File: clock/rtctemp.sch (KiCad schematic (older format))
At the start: 15 parts, among them U601 ADT7410, U602 DS3231, U603 ADT7410

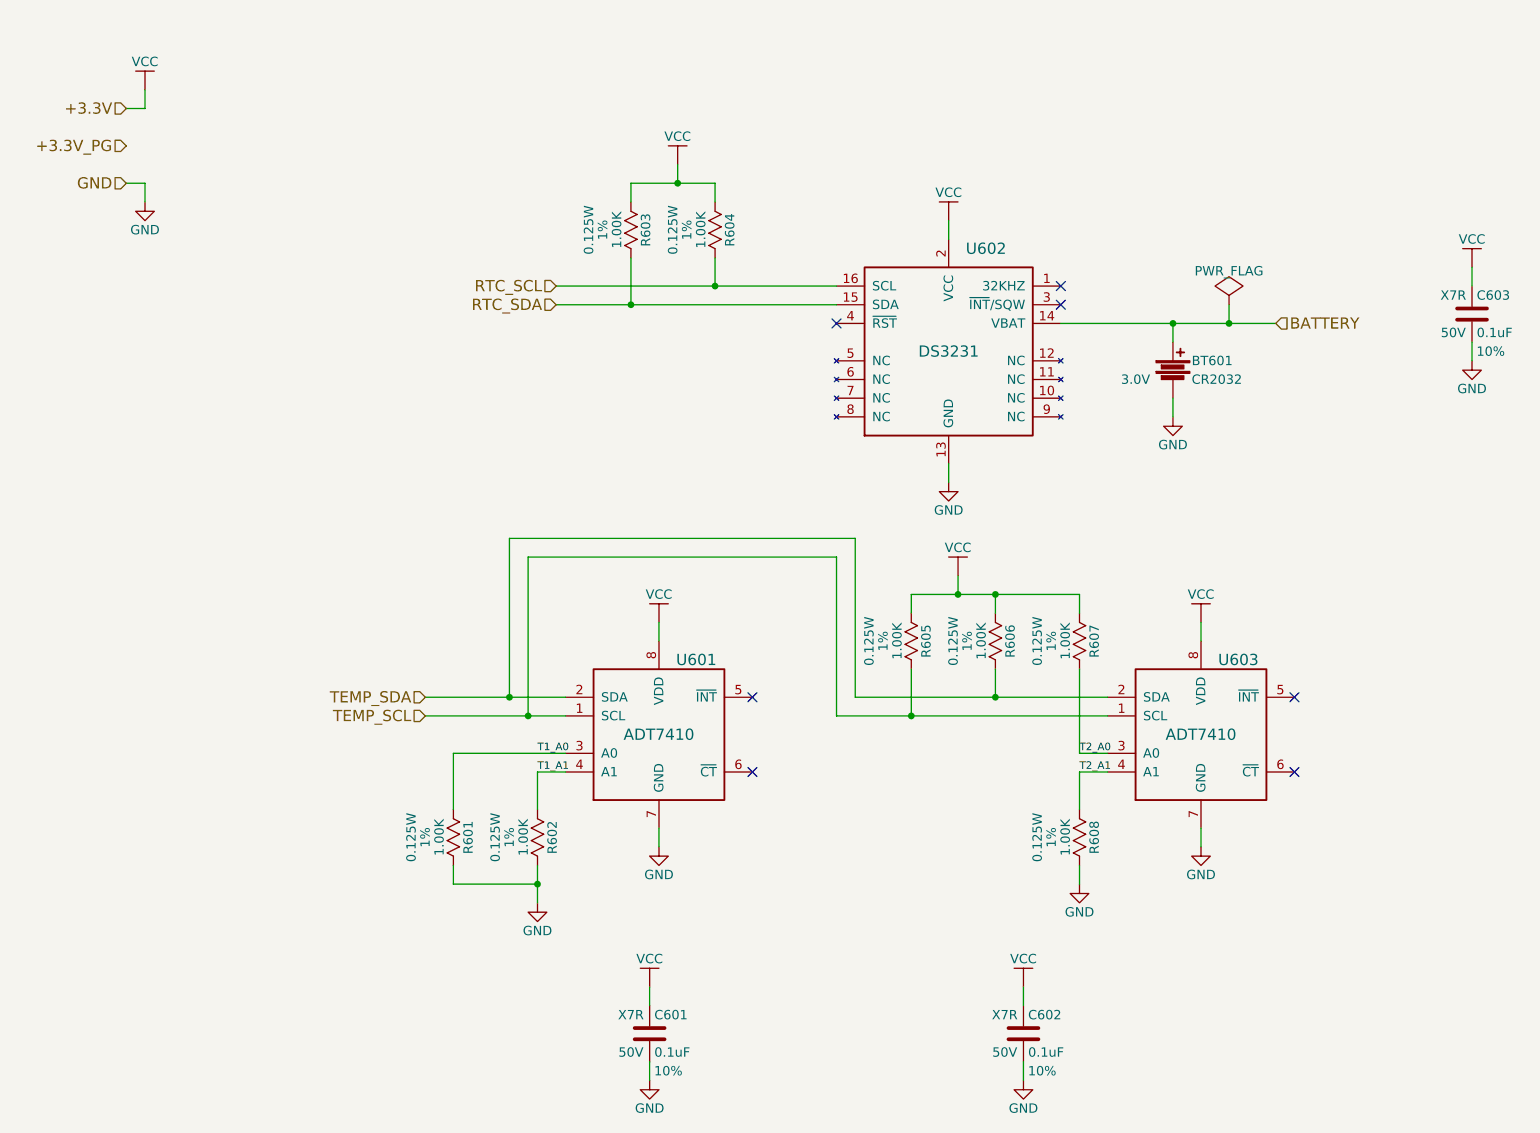
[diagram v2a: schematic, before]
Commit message: Preliminary changes from lab bring up.   Properly connect ref2 on PCA9306.   Duplicate +5V power good to drive +3.3V converter.   Change gain structure on OCXO control voltage drive.   Add FET control to disable linear regulators.
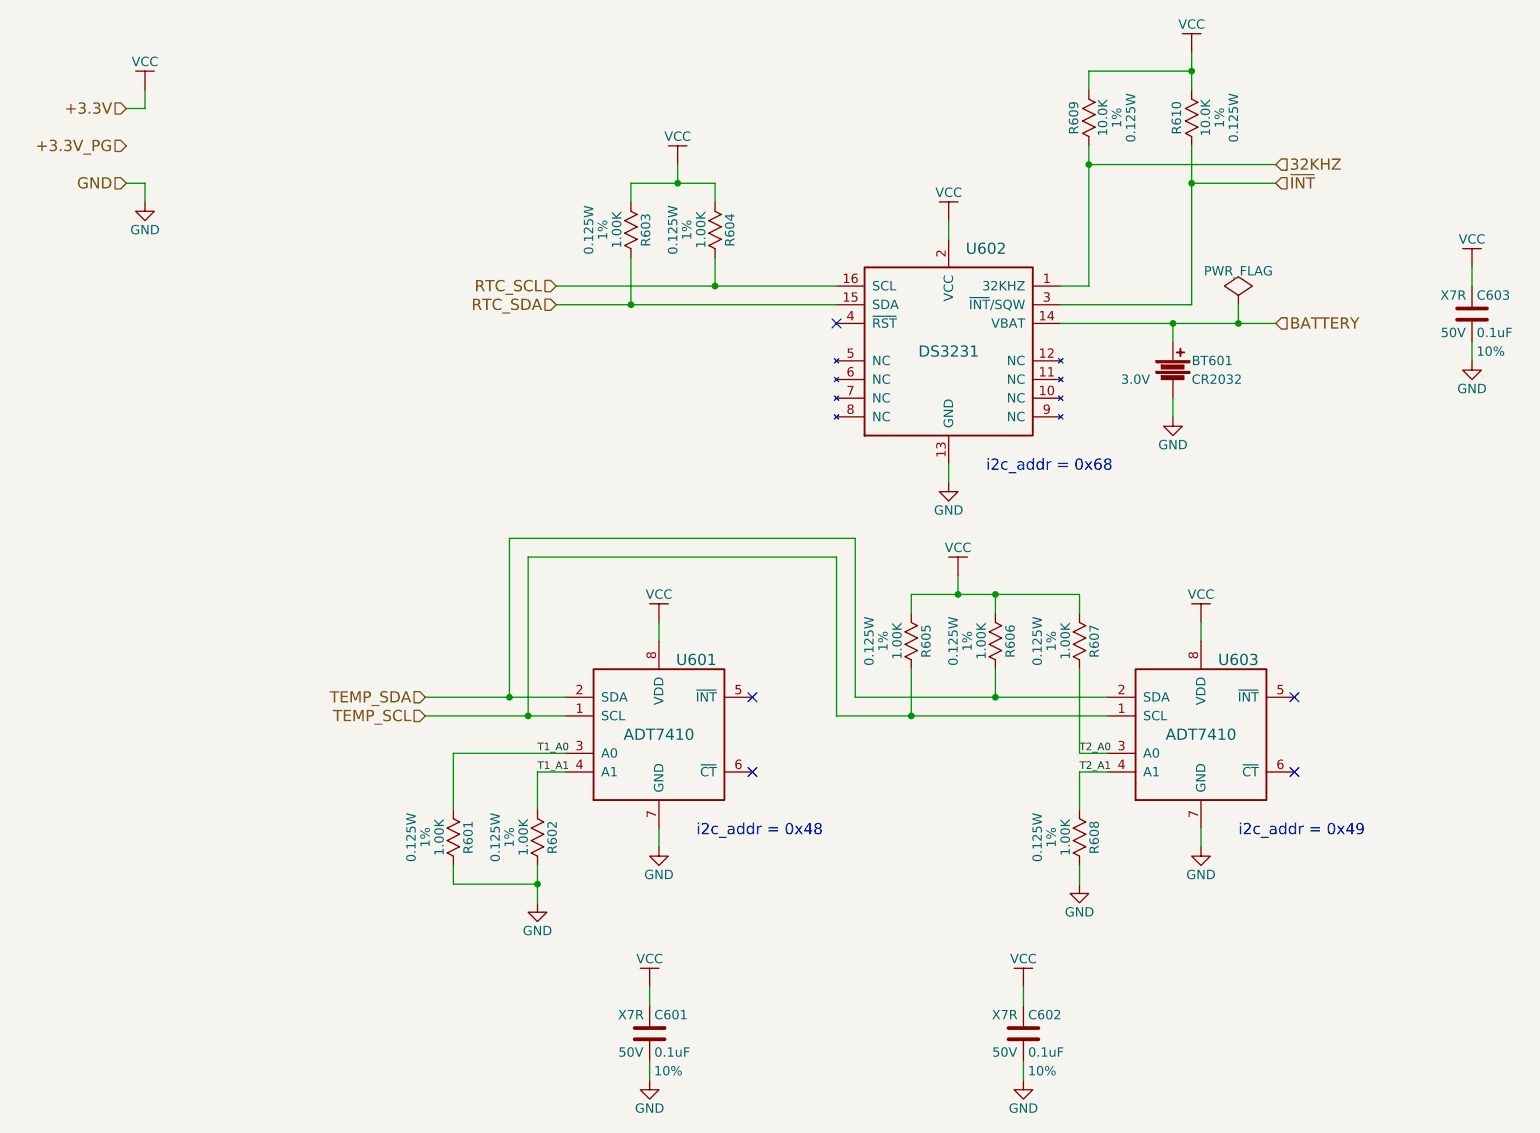
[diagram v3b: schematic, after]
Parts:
- added R609, R610: 10.0K, Resistors_SMD:R_0805_HandSoldering, symbol R_local
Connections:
- net VCC: now also R609.2, R610.2
- net 32KHZ: now reaches U602.1 (32KHZ)
- net 32KHZ: now also R609.1
- net ~INT~: now reaches U602.3 (~INT~/SQW)
- net ~INT~: now also R610.1
- no-connect marks 7 -> 5
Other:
- note added: "i2c_addr = 0x48"
- note added: "i2c_addr = 0x49"
- note added: "i2c_addr = 0x68"
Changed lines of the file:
@@
 RTC_SDA
 $Comp
-L GND #PWR078
+L GND #PWR602
 U 1 1 5636B600
 P 1450 1900
-F 0 "#PWR078" H 1450 1650 50  0001 C CNN
+F 0 "#PWR602" H 1450 1650 50  0001 C CNN
 F 1 "GND" H 1450 1750 50  0000 C CNN
 F 2 "" H 1450 1900 60  0000 C CNN
@@
 	5750 3400 5750 3300
 $Comp
-L GND #PWR079
+L GND #PWR610
 U 1 1 5636B6C4
 P 5750 3400
-F 0 "#PWR079" H 5750 3150 50  0001 C CNN
+F 0 "#PWR610" H 5750 3150 50  0001 C CNN
 F 1 "GND" H 5750 3250 50  0000 C CNN
 F 2 "" H 5750 3400 60  0000 C CNN
@@
 $EndComp
 $Comp
-L VCC #PWR080
+L VCC #PWR601
 U 1 1 5636B791
 P 1450 1300
-F 0 "#PWR080" H 1450 1150 50  0001 C CNN
+F 0 "#PWR601" H 1450 1150 50  0001 C CNN
 F 1 "VCC" H 1450 1450 50  0000 C CNN
 F 2 "" H 1450 1300 60  0000 C CNN
@@
 	1450 1400 1450 1300
 $Comp
-L VCC #PWR081
+L VCC #PWR609
 U 1 1 5636B7D2
 P 5750 2000
-F 0 "#PWR081" H 5750 1850 50  0001 C CNN
+F 0 "#PWR609" H 5750 1850 50  0001 C CNN
 F 1 "VCC" H 5750 2150 50  0000 C CNN
 F 2 "" H 5750 2000 60  0000 C CNN
@@
 	4500 1800 4500 1900
 $Comp
-L VCC #PWR082
+L VCC #PWR608
 U 1 1 5636BBAE
 P 4300 1700
-F 0 "#PWR082" H 4300 1550 50  0001 C CNN
+F 0 "#PWR608" H 4300 1550 50  0001 C CNN
 F 1 "VCC" H 4300 1850 50  0000 C CNN
 F 2 "" H 4300 1700 60  0000 C CNN
@@
 	6950 2550 6950 2650
 $Comp
-L GND #PWR083
+L GND #PWR615
 U 1 1 5636BC94
 P 6950 3050
-F 0 "#PWR083" H 6950 2800 50  0001 C CNN
+F 0 "#PWR615" H 6950 2800 50  0001 C CNN
 F 1 "GND" H 6950 2900 50  0000 C CNN
 F 2 "" H 6950 3050 60  0000 C CNN
@@
 $EndComp
 $Comp
-L VCC #PWR084
+L VCC #PWR606
 U 1 1 5636C0D5
 P 4200 4150
-F 0 "#PWR084" H 4200 4000 50  0001 C CNN
+F 0 "#PWR606" H 4200 4000 50  0001 C CNN
 F 1 "VCC" H 4200 4300 50  0000 C CNN
 F 2 "" H 4200 4150 60  0000 C CNN
@@
 	7100 5350 7100 5250
 $Comp
-L GND #PWR085
+L GND #PWR618
 U 1 1 5636C104
 P 7100 5350
-F 0 "#PWR085" H 7100 5100 50  0001 C CNN
+F 0 "#PWR618" H 7100 5100 50  0001 C CNN
 F 1 "GND" H 7100 5200 50  0000 C CNN
 F 2 "" H 7100 5350 60  0000 C CNN
@@
 	4200 5350 4200 5250
 $Comp
-L GND #PWR086
+L GND #PWR607
 U 1 1 5636C11B
 P 4200 5350
-F 0 "#PWR086" H 4200 5100 50  0001 C CNN
+F 0 "#PWR607" H 4200 5100 50  0001 C CNN
 F 1 "GND" H 4200 5200 50  0000 C CNN
 F 2 "" H 4200 5350 60  0000 C CNN
@@
 	6000 4000 6000 4100
 $Comp
-L VCC #PWR087
+L VCC #PWR611
 U 1 1 5636C1AA
 P 5800 3900
-F 0 "#PWR087" H 5800 3750 50  0001 C CNN
+F 0 "#PWR611" H 5800 3750 50  0001 C CNN
 F 1 "VCC" H 5800 4050 50  0000 C CNN
 F 2 "" H 5800 3900 60  0000 C CNN
@@
 Connection ~ 3550 5550
 $Comp
-L GND #PWR088
+L GND #PWR603
 U 1 1 5636C550
 P 3550 5650
-F 0 "#PWR088" H 3550 5400 50  0001 C CNN
+F 0 "#PWR603" H 3550 5400 50  0001 C CNN
 F 1 "GND" H 3550 5500 50  0000 C CNN
 F 2 "" H 3550 5650 60  0000 C CNN
@@
 	6450 4950 6450 5150
 $Comp
-L GND #PWR089
+L GND #PWR614
 U 1 1 5636C5CD
 P 6450 5550
-F 0 "#PWR089" H 6450 5300 50  0001 C CNN
+F 0 "#PWR614" H 6450 5300 50  0001 C CNN
 F 1 "GND" H 6450 5400 50  0000 C CNN
 F 2 "" H 6450 5550 60  0000 C CNN
@@
 Connection ~ 3500 4650
 $Comp
-L GND #PWR090
+L GND #PWR620
 U 1 1 5636CF30
 P 8550 2750
-F 0 "#PWR090" H 8550 2500 50  0001 C CNN
+F 0 "#PWR620" H 8550 2500 50  0001 C CNN
 F 1 "GND" H 8550 2600 50  0000 C CNN
 F 2 "" H 8550 2750 60  0000 C CNN
@@
 $EndComp
 $Comp
-L VCC #PWR091
+L VCC #PWR619
 U 1 1 5636D2DE
 P 8550 2250
-F 0 "#PWR091" H 8550 2100 50  0001 C CNN
+F 0 "#PWR619" H 8550 2100 50  0001 C CNN
 F 1 "VCC" H 8550 2400 50  0000 C CNN
 F 2 "" H 8550 2250 60  0000 C CNN
@@
 $EndComp
 $Comp
-L GND #PWR092
+L GND #PWR605
 U 1 1 5636D43C
 P 4150 6600
-F 0 "#PWR092" H 4150 6350 50  0001 C CNN
+F 0 "#PWR605" H 4150 6350 50  0001 C CNN
 F 1 "GND" H 4150 6450 50  0000 C CNN
 F 2 "" H 4150 6600 60  0000 C CNN
@@
 $EndComp
 $Comp
-L VCC #PWR093
+L VCC #PWR604
 U 1 1 5636D44F
 P 4150 6100
-F 0 "#PWR093" H 4150 5950 50  0001 C CNN
+F 0 "#PWR604" H 4150 5950 50  0001 C CNN
 F 1 "VCC" H 4150 6250 50  0000 C CNN
 F 2 "" H 4150 6100 60  0000 C CNN
@@
 $EndComp
 $Comp
-L GND #PWR094
+L GND #PWR613
 U 1 1 5636D49F
 P 6150 6600
-F 0 "#PWR094" H 6150 6350 50  0001 C CNN
+F 0 "#PWR613" H 6150 6350 50  0001 C CNN
 F 1 "GND" H 6150 6450 50  0000 C CNN
 F 2 "" H 6150 6600 60  0000 C CNN
@@
 $EndComp
 $Comp
-L VCC #PWR095
+L VCC #PWR612
 U 1 1 5636D4B2
 P 6150 6100
-F 0 "#PWR095" H 6150 5950 50  0001 C CNN
+F 0 "#PWR612" H 6150 5950 50  0001 C CNN
 F 1 "VCC" H 6150 6250 50  0000 C CNN
 F 2 "" H 6150 6100 60  0000 C CNN
@@
 NoConn ~ 7600 4550
 NoConn ~ 5150 2550
-NoConn ~ 6350 2450
-NoConn ~ 6350 2350
-$Comp
-L VCC #PWR096
+$Comp
+L VCC #PWR617
 U 1 1 563E1DA8
 P 7100 4150
-F 0 "#PWR096" H 7100 4000 50  0001 C CNN
+F 0 "#PWR617" H 7100 4000 50  0001 C CNN
 F 1 "VCC" H 7100 4300 50  0000 C CNN
 F 2 "" H 7100 4150 60  0000 C CNN
@@
 	6450 5550 6450 5450
 $Comp
-L PWR_FLAG #FLG097
+L PWR_FLAG #FLG601
 U 1 1 564556C2
-P 7250 2450
-F 0 "#FLG097" H 7250 2545 50  0001 C CNN
-F 1 "PWR_FLAG" H 7250 2630 50  0000 C CNN
-F 2 "" H 7250 2450 60  0000 C CNN
-F 3 "" H 7250 2450 60  0000 C CNN
-	1    7250 2450
-	1    0    0    -1
-$EndComp
-Wire Wire Line
-	7250 2450 7250 2550
-Connection ~ 7250 2550
+P 7300 2450
+F 0 "#FLG601" H 7300 2545 50  0001 C CNN
+F 1 "PWR_FLAG" H 7300 2630 50  0000 C CNN
+F 2 "" H 7300 2450 60  0000 C CNN
+F 3 "" H 7300 2450 60  0000 C CNN
+	1    7300 2450
+	1    0    0    -1
+$EndComp
+Wire Wire Line
+	7300 2450 7300 2550
+Connection ~ 7300 2550
+$Comp
+L R_local R609
+U 1 1 57AC1154
+P 6500 1450
+F 0 "R609" V 6580 1450 50  0000 C CNN
+F 1 "10.0K" V 6425 1450 50  0000 C CNN
+F 2 "Resistors_SMD:R_0805_HandSoldering" V 6430 1450 30  0001 C CNN
+F 3 "" V 6580 1450 30  0000 C CNN
+F 4 "1%" V 6350 1450 50  0000 C CNN "Tolerance"
+F 5 "0.125W" V 6275 1450 50  0000 C CNN "Power"
+F 6 "Vishay Dale" V 6500 1450 50  0001 C CNN "Manufacturer"
+F 7 "CRCW080510K0FKEA" V 6650 1450 50  0001 C CNN "PartNum"
+	1    6500 1450
+	-1   0    0    1
+$EndComp
+$Comp
+L R_local R610
+U 1 1 57AC1181
+P 7050 1450
+F 0 "R610" V 7130 1450 50  0000 C CNN
+F 1 "10.0K" V 6975 1450 50  0000 C CNN
+F 2 "Resistors_SMD:R_0805_HandSoldering" V 6980 1450 30  0001 C CNN
+F 3 "" V 7130 1450 30  0000 C CNN
+F 4 "1%" V 6900 1450 50  0000 C CNN "Tolerance"
+F 5 "0.125W" V 6825 1450 50  0000 C CNN "Power"
+F 6 "Vishay Dale" V 7050 1450 50  0001 C CNN "Manufacturer"
+F 7 "CRCW080510K0FKEA" V 7200 1450 50  0001 C CNN "PartNum"
+	1    7050 1450
+	-1   0    0    1
+$EndComp
+Text HLabel 7500 1700 2    60   Input ~ 0
+32KHZ
+Text HLabel 7500 1800 2    60   Input ~ 0
+~INT~
+Wire Wire Line
+	7050 2450 6350 2450
+Wire Wire Line
+	7050 1600 7050 2450
+Wire Wire Line
+	7050 1800 7500 1800
+Wire Wire Line
+	6500 2350 6350 2350
+Wire Wire Line
+	6500 1600 6500 2350
+Wire Wire Line
+	6500 1700 7500 1700
+Wire Wire Line
+	6500 1300 6500 1200
+Wire Wire Line
+	6500 1200 7050 1200
+Wire Wire Line
+	7050 1100 7050 1300
+Connection ~ 7050 1800
+Connection ~ 6500 1700
+$Comp
+L VCC #PWR616
+U 1 1 57AC17FC
+P 7050 1100
+F 0 "#PWR616" H 7050 950 50  0001 C CNN
+F 1 "VCC" H 7050 1250 50  0000 C CNN
+F 2 "" H 7050 1100 60  0000 C CNN
+F 3 "" H 7050 1100 60  0000 C CNN
+	1    7050 1100
+	1    0    0    -1
+$EndComp
+Connection ~ 7050 1200
+Text Notes 5950 3350 0    60   ~ 0
+i2c_addr = 0x68
+Text Notes 4400 5300 0    60   ~ 0
+i2c_addr = 0x48
+Text Notes 7300 5300 0    60   ~ 0
+i2c_addr = 0x49
 $EndSCHEMATC
